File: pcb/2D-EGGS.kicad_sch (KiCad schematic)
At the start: 41 parts, among them J1 BUTTON 1, J10 EFFECT, J11 AUX, J12 USB_B, J13 PWAN1, J14 PWAN2, J15 ENCODER, J16 GPIO, J2 BUTTON 2, J3 BUTTON 3, J4 BUTTON 4, J5 BUTTON 5, J6 BUTTON 6, J7 BUTTON 7, J8 START, J9 VEFX, Q1 2N7000, Q10 2N7000, Q11 2N7000, Q2 2N7000, Q3 2N7000, Q4 2N7000, Q5 2N7000, Q6 2N7000, Q7 2N7000, Q8 2N7000, Q9 2N7000, SW1 SW_Push, U1 AT90USB1286, Y1 16MHz

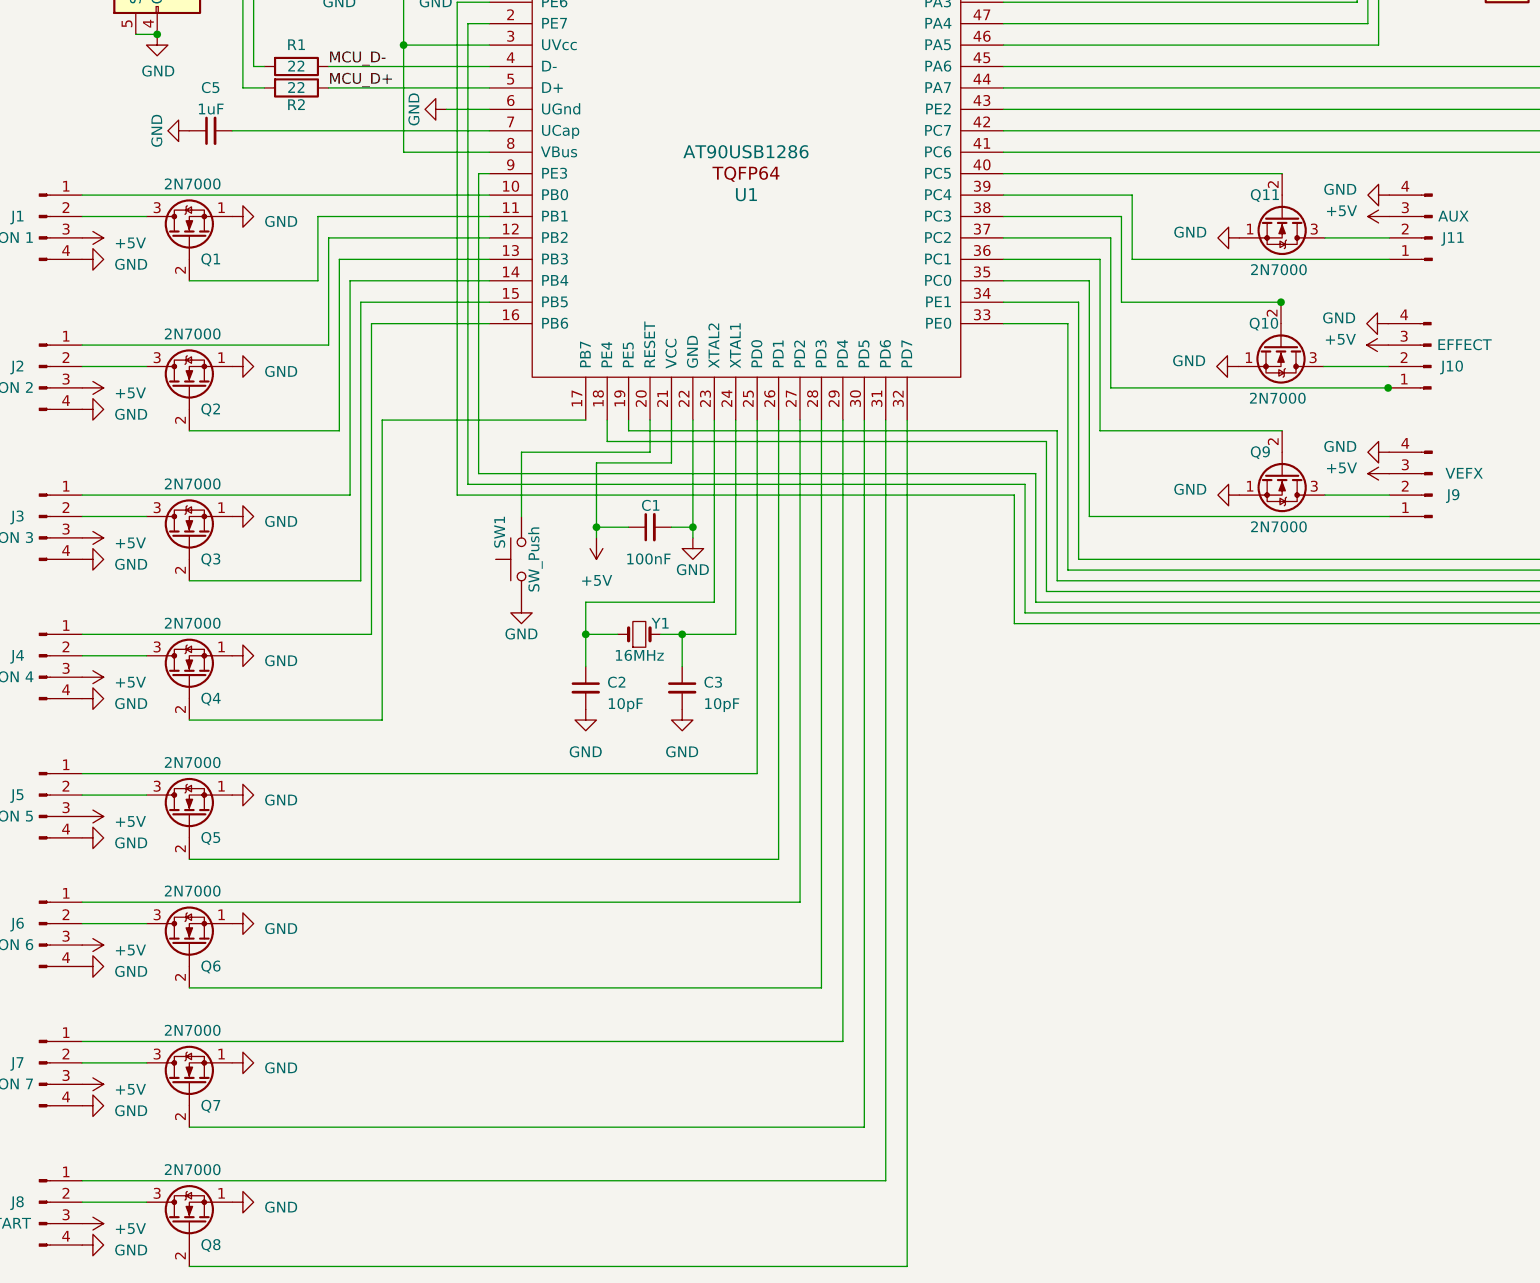
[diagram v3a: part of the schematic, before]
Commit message: 2N7000 -> 2N7002. add series resistor to reset switch
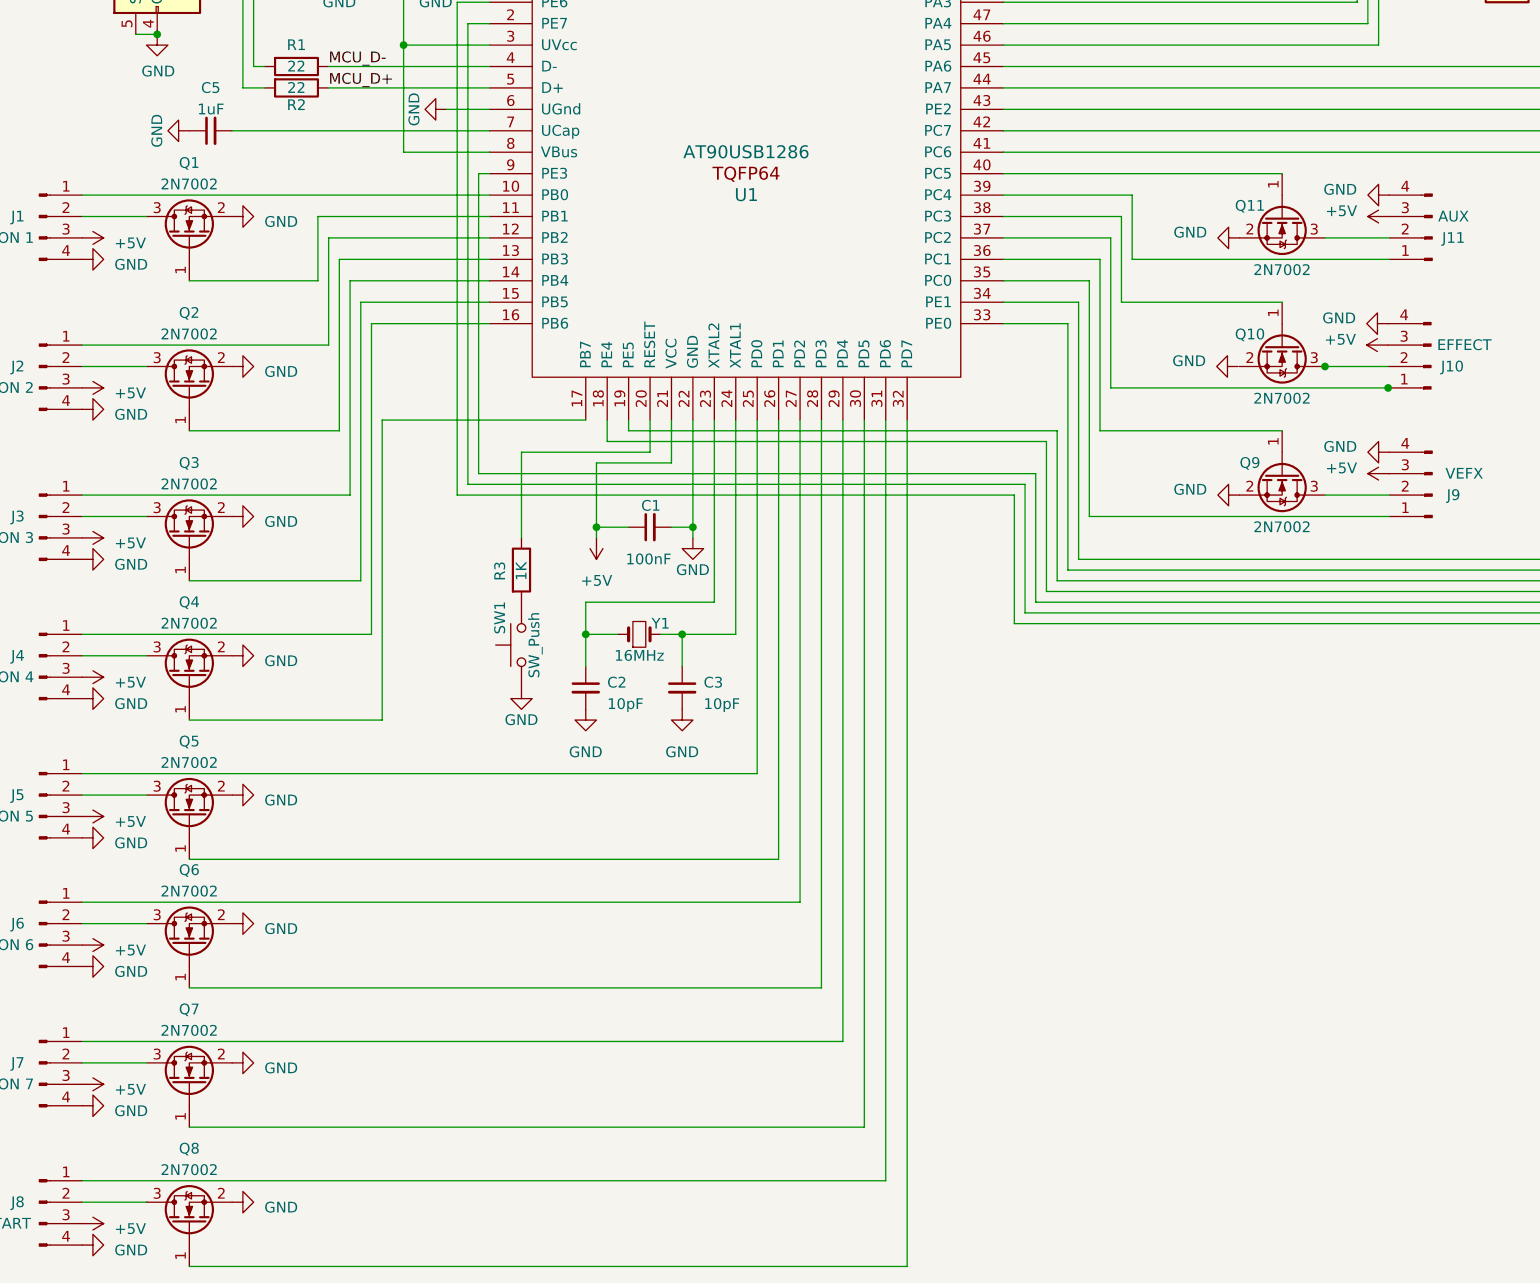
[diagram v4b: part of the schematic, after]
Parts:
- removed Q1, Q10, Q11, Q2, Q3, Q4, Q5, Q6, Q7, Q8, Q9: 2N7000, Package_TO_SOT_THT:TO-92_Inline, symbol Transistor_FET:2N7000
- added Q1, Q10, Q11, Q2, Q3, Q4, Q5, Q6, Q7, Q8, Q9: 2N7002, Package_TO_SOT_SMD:SOT-23, symbol Transistor_FET:2N7002
- added R3: 1K, Resistor_SMD:R_0805_2012Metric, symbol Device:R
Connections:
- net GND: now also Q1.2 (S), Q11.2 (S), Q2.2 (S), Q3.2 (S), Q4.2 (S), Q5.2 (S), Q6.2 (S), Q7.2 (S), Q8.2 (S), Q9.2 (S)
- net at J7.2 (Pin_2): now also Q7.3 (D)
- net at J2.2 (Pin_2): now also Q2.3 (D)
- net at J6.2 (Pin_2): now also Q6.3 (D)
- net at U1.15 (PB5): now also Q3.1 (G)
- net at J3.2 (Pin_2): now also Q3.3 (D)
- net at U1.38 (PC3): now also Q10.1 (G)
- net at J10.2 (Pin_2): now also Q10.3 (D)
- net at U1.28 (PD3): now also Q6.1 (G)
- net at J4.2 (Pin_2): now also Q4.3 (D)
- net at U1.40 (PC5): now also Q11.1 (G)
- net at J11.2 (Pin_2): now also Q11.3 (D)
- net at J9.2 (Pin_2): now also Q9.3 (D)
- net at U1.11 (PB1): now also Q1.1 (G)
- net at U1.13 (PB3): now also Q2.1 (G)
- net at U1.17 (PB7): now also Q4.1 (G)
- net at U1.20 (RESET): now also R3.1; no longer SW1.2
- net at U1.26 (PD1): now also Q5.1 (G)
- net at U1.30 (PD5): now also Q7.1 (G)
- net at U1.32 (PD7): now also Q8.1 (G)
- net at U1.36 (PC1): now also Q9.1 (G)
- net at J1.2 (Pin_2): now also Q1.3 (D)
- net at J5.2 (Pin_2): now also Q5.3 (D)
- net at J8.2 (Pin_2): now also Q8.3 (D)
- new net: R3.2, SW1.2
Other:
- moved on the sheet: SW1

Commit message: update schematic, pcb layout WIP
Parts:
- removed J1: BUTTON 1, Connector_JST:JST_XH_B4B-XH-A_1x04_P2.50mm_Vertical, symbol Connector:Conn_01x04_Pin
- removed J12: USB_B, Connector_USB:USB_B_OST_USB-B1HSxx_Horizontal, symbol jamma-streamer-rescue:USB_B-Connector
- removed J16: GPIO, Connector_PinHeader_2.54mm:PinHeader_2x12_P2.54mm_Vertical, symbol Connector_Generic:Conn_02x12_Counter_Clockwise
- removed J2: BUTTON 2, Connector_JST:JST_XH_B4B-XH-A_1x04_P2.50mm_Vertical, symbol Connector:Conn_01x04_Pin
- removed Q1, Q2: 2N7002, Package_TO_SOT_SMD:SOT-23, symbol Transistor_FET:2N7002
- added J1: ISP, Connector_PinHeader_2.54mm:PinHeader_2x03_P2.54mm_Vertical, symbol Connector_Generic:Conn_02x03_Odd_Even
- added J12: PWAN_CENTER_LED, Connector_JST:JST_XH_B3B-XH-A_1x03_P2.50mm_Vertical, symbol Connector:Conn_01x03_Pin
- added J16: DBG_PWR, Connector_PinHeader_2.54mm:PinHeader_1x02_P2.54mm_Vertical, symbol Connector_Generic:Conn_01x02
- added J17: PWAN_E2P1, Connector_JST:JST_XH_B3B-XH-A_1x03_P2.50mm_Vertical, symbol Connector:Conn_01x03_Pin
- added J18: PWAN_E2P2, Connector_JST:JST_XH_B3B-XH-A_1x03_P2.50mm_Vertical, symbol Connector:Conn_01x03_Pin
- added J19: ENCODER2, Connector_JST:JST_XH_B4B-XH-A_1x04_P2.50mm_Vertical, symbol Connector:Conn_01x04_Pin
- added J2: TT_LED, Connector_JST:JST_XH_B3B-XH-A_1x03_P2.50mm_Vertical, symbol Connector:Conn_01x03_Pin
- added J20: B10, Connector_JST:JST_XH_B4B-XH-A_1x04_P2.50mm_Vertical, symbol Connector:Conn_01x04_Pin
- added J21: B11, Connector_JST:JST_XH_B4B-XH-A_1x04_P2.50mm_Vertical, symbol Connector:Conn_01x04_Pin
- added J22: PWAN_USB_B, Connector_JST:JST_XH_B5B-XH-A_1x05_P2.50mm_Vertical, symbol Connector_Generic:Conn_01x05
- added J23: PWAN_USB_C, Connector_JST:JST_PH_B2B-PH-K_1x02_P2.00mm_Vertical, symbol Connector_Generic:Conn_01x02
- added J24: LED1, Connector_JST:JST_XH_B2B-XH-A_1x02_P2.50mm_Vertical, symbol Connector_Generic:Conn_01x02
- added J25: LED2, Connector_JST:JST_XH_B2B-XH-A_1x02_P2.50mm_Vertical, symbol Connector_Generic:Conn_01x02
- added P1: USB_C_DATA, Connector_USB:USB_C_Receptacle_GCT_USB4085, symbol Connector:USB_C_Plug
- added P2: USB_C_POWER, Connector_USB:USB_C_Receptacle_GCT_USB4085, symbol Connector:USB_C_Plug
- added Q12, Q13: 2N7002, Package_TO_SOT_SMD:SOT-23, symbol Transistor_FET:2N7002
- added R4: 4.7K, Resistor_SMD:R_0805_2012Metric, symbol Device:R
- J10: value EFFECT -> B8
- J11: value AUX -> B9
- J13: value PWAN1 -> PWAN_E1P1
- J14: value PWAN2 -> PWAN_E1P2
- J15: value ENCODER -> ENCODER1
- J3: value BUTTON 3 -> B1
- J4: value BUTTON 4 -> B2
- J5: value BUTTON 5 -> B3
- J6: value BUTTON 6 -> B4
- J7: value BUTTON 7 -> B5
- J8: value START -> B6
- J9: value VEFX -> B7
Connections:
- net +5V: now also J15.2 (Pin_2), J1.2 (Pin_2), J12.2 (Pin_2), J16.1 (Pin_1), J17.3 (Pin_3), J18.3 (Pin_3), J19.2 (Pin_2), J2.2 (Pin_2), J20.3 (Pin_3), J21.3 (Pin_3), J22.5 (Pin_5), J23.2 (Pin_2), J24.2 (Pin_2), J25.2 (Pin_2), P1.A4 (VBUS), P1.A9 (VBUS), P1.B4 (VBUS), P1.B9 (VBUS), P2.A4 (VBUS), P2.A9 (VBUS), P2.B4 (VBUS), P2.B9 (VBUS), R4.2; no longer J15.3 (Pin_3)
- net GND: now also J15.1 (Pin_1), J1.6 (Pin_6), J12.3 (Pin_3), J16.2 (Pin_2), J17.2 (Pin_2), J18.2 (Pin_2), J19.1 (Pin_1), J2.3 (Pin_3), J20.4 (Pin_4), J21.4 (Pin_4), J22.1 (Pin_1), J22.2 (Pin_2), J23.1 (Pin_1), J24.1 (Pin_1), J25.1 (Pin_1), P1.A1 (GND), P1.A12 (GND), P1.B1 (GND), P1.B12 (GND), P1.S1 (SHIELD), P2.A1 (GND), P2.A12 (GND), P2.B1 (GND), P2.B12 (GND), P2.S1 (SHIELD), Q12.2 (S), Q13.2 (S); no longer J15.4 (Pin_4)
- net USB-R_D+: now also J22.3 (Pin_3), P1.A6 (D+)
- net USB-R_D-: now also J22.4 (Pin_4), P1.A7 (D-)
- net at U1.12 (PB2_MOSI): now also J1.4 (Pin_4)
- net at J13.1 (Pin_1), U1.61 (PF0): now also J15.4 (Pin_4); no longer J15.1 (Pin_1)
- net at J14.1 (Pin_1), U1.60 (PF1): now also J15.3 (Pin_3); no longer J15.2 (Pin_2)
- net at Q10.1 (G): now also U1.36 (PC1); no longer U1.38 (PC3)
- net at J9.1 (Pin_1): now also U1.33 (PE0); no longer U1.35 (PC0)
- net at U1.11 (PB1_SCLK): now also J1.3 (Pin_3)
- net at U1.13 (PB3_MISO): now also J1.1 (Pin_1)
- net at R3.1, U1.20 (RESET): now also J1.5 (Pin_5), R4.1
- net at U1.34 (PE1): now also Q9.1 (G)
- net at J10.1 (Pin_1): now also U1.35 (PC0); no longer U1.37 (PC2)
- net at U1.39 (PC4): now also J12.1 (Pin_1); no longer J11.1 (Pin_1)
- net at Q11.1 (G): now also U1.38 (PC3); no longer U1.40 (PC5)
- net at U1.43 (PE2): now also J20.1 (Pin_1)
- net at U1.44 (PA7): now also Q12.1 (G)
- net at U1.45 (PA6): now also J21.1 (Pin_1)
- net at U1.46 (PA5): now also Q13.1 (G)
- net at U1.58 (PF3): now also J18.1 (Pin_1), J19.3 (Pin_3)
- net at U1.59 (PF2): now also J17.1 (Pin_1), J19.4 (Pin_4)
- new net: J20.2 (Pin_2), Q12.3 (D)
- new net: J21.2 (Pin_2), Q13.3 (D)
- new net: J11.1 (Pin_1), U1.37 (PC2)
- new net: J2.1 (Pin_1), U1.40 (PC5)
- no-connect marks 0 -> 43
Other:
- moved on the sheet: C1, C2, C3, C4, C5, C6, C7, C8, C9, J10, J11, J13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

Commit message: v2 routed
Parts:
- added J26: APWR, Connector_PinHeader_2.54mm:PinHeader_1x02_P2.54mm_Vertical, symbol Connector_Generic:Conn_01x02
- J16: value DBG_PWR -> DPWR
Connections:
- net +5V: now also J26.1 (Pin_1)
- net GND: now also J26.2 (Pin_2)
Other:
- moved on the sheet: J16
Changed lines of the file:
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@@
     )
   )
-  (symbol (lib_id "power:GND") (at 247.65 194.31 90) (unit 1)
-    (in_bom yes) (on_board yes) (dnp no) (fields_autoplaced)
-    (property "Reference" "#PWR072" (at 254 194.31 0)
-      (effects (font (size 1.27 1.27)) hide)
-    )
-    (property "Value" "GND" (at 251.46 193.675 90)
-      (effects (font (size 1.27 1.27)) (justify right))
-    )
-    (property "Footprint" "" (at 247.65 194.31 0)
-      (effects (font (size 1.27 1.27)) hide)
-    )
-    (property "Datasheet" "" (at 247.65 194.31 0)
+  (symbol (lib_id "power:GND") (at 247.65 195.58 90) (unit 1)
+    (in_bom yes) (on_board yes) (dnp no) (fields_autoplaced)
+    (property "Reference" "#PWR072" (at 254 195.58 0)
+      (effects (font (size 1.27 1.27)) hide)
+    )
+    (property "Value" "GND" (at 251.46 194.945 90)
+      (effects (font (size 1.27 1.27)) (justify right))
+    )
+    (property "Footprint" "" (at 247.65 195.58 0)
+      (effects (font (size 1.27 1.27)) hide)
+    )
+    (property "Datasheet" "" (at 247.65 195.58 0)
       (effects (font (size 1.27 1.27)) hide)
     )
@@
     )
   )
+  (symbol (lib_id "Connector_Generic:Conn_01x02") (at 242.57 189.23 180) (unit 1)
+    (in_bom yes) (on_board yes) (dnp no)
+    (property "Reference" "J26" (at 242.57 184.15 0)
+      (effects (font (size 1.27 1.27)))
+    )
+    (property "Value" "APWR" (at 237.49 187.96 0)
+      (effects (font (size 1.27 1.27)))
+    )
+    (property "Footprint" "Connector_PinHeader_2.54mm:PinHeader_1x02_P2.54mm_Vertical" (at 242.57 189.23 0)
+      (effects (font (size 1.27 1.27)) hide)
+    )
+    (property "Datasheet" "~" (at 242.57 189.23 0)
+      (effects (font (size 1.27 1.27)) hide)
+    )
+    (pin "1")
+    (pin "2")
+    (instances
+      (project "2D-EGGS"
+        (path "/603cab36-5bc1-4050-9595-d50dcdf15559"
+          (reference "J26") (unit 1)
+        )
+      )
+    )
+  )
+  (symbol (lib_id "power:+5V") (at 247.65 189.23 270) (unit 1)
+    (in_bom yes) (on_board yes) (dnp no) (fields_autoplaced)
+    (property "Reference" "#PWR084" (at 243.84 189.23 0)
+      (effects (font (size 1.27 1.27)) hide)
+    )
+    (property "Value" "+5V" (at 251.46 189.865 90)
+      (effects (font (size 1.27 1.27)) (justify left))
+    )
+    (property "Footprint" "" (at 247.65 189.23 0)
+      (effects (font (size 1.27 1.27)) hide)
+    )
+    (property "Datasheet" "" (at 247.65 189.23 0)
+      (effects (font (size 1.27 1.27)) hide)
+    )
+    (pin "1")
+    (instances
+      (project "2D-EGGS"
+        (path "/603cab36-5bc1-4050-9595-d50dcdf15559"
+          (reference "#PWR084") (unit 1)
+        )
+      )
+    )
+  )
+  (symbol (lib_id "power:GND") (at 247.65 186.69 90) (unit 1)
+    (in_bom yes) (on_board yes) (dnp no) (fields_autoplaced)
+    (property "Reference" "#PWR083" (at 254 186.69 0)
+      (effects (font (size 1.27 1.27)) hide)
+    )
+    (property "Value" "GND" (at 251.46 186.055 90)
+      (effects (font (size 1.27 1.27)) (justify right))
+    )
+    (property "Footprint" "" (at 247.65 186.69 0)
+      (effects (font (size 1.27 1.27)) hide)
+    )
+    (property "Datasheet" "" (at 247.65 186.69 0)
+      (effects (font (size 1.27 1.27)) hide)
+    )
+    (pin "1")
+    (instances
+      (project "2D-EGGS"
+        (path "/603cab36-5bc1-4050-9595-d50dcdf15559"
+          (reference "#PWR083") (unit 1)
+        )
+      )
+    )
+  )
   (symbol (lib_id "power:+5V") (at 217.17 68.58 180) (unit 1)
     (in_bom yes) (on_board yes) (dnp no)
@@
     )
   )
-  (symbol (lib_id "power:+5V") (at 247.65 196.85 270) (unit 1)
-    (in_bom yes) (on_board yes) (dnp no) (fields_autoplaced)
-    (property "Reference" "#PWR073" (at 243.84 196.85 0)
-      (effects (font (size 1.27 1.27)) hide)
-    )
-    (property "Value" "+5V" (at 251.46 197.485 90)
-      (effects (font (size 1.27 1.27)) (justify left))
-    )
-    (property "Footprint" "" (at 247.65 196.85 0)
-      (effects (font (size 1.27 1.27)) hide)
-    )
-    (property "Datasheet" "" (at 247.65 196.85 0)
+  (symbol (lib_id "power:+5V") (at 247.65 198.12 270) (unit 1)
+    (in_bom yes) (on_board yes) (dnp no) (fields_autoplaced)
+    (property "Reference" "#PWR073" (at 243.84 198.12 0)
+      (effects (font (size 1.27 1.27)) hide)
+    )
+    (property "Value" "+5V" (at 251.46 198.755 90)
+      (effects (font (size 1.27 1.27)) (justify left))
+    )
+    (property "Footprint" "" (at 247.65 198.12 0)
+      (effects (font (size 1.27 1.27)) hide)
+    )
+    (property "Datasheet" "" (at 247.65 198.12 0)
       (effects (font (size 1.27 1.27)) hide)
     )
@@
     )
   )
-  (symbol (lib_id "Connector_Generic:Conn_01x02") (at 242.57 196.85 180) (unit 1)
-    (in_bom yes) (on_board yes) (dnp no) (fields_autoplaced)
-    (property "Reference" "J16" (at 240.03 196.215 0)
-      (effects (font (size 1.27 1.27)) (justify left))
-    )
-    (property "Value" "DBG_PWR" (at 240.03 193.675 0)
-      (effects (font (size 1.27 1.27)) (justify left))
-    )
-    (property "Footprint" "Connector_PinHeader_2.54mm:PinHeader_1x02_P2.54mm_Vertical" (at 242.57 196.85 0)
-      (effects (font (size 1.27 1.27)) hide)
-    )
-    (property "Datasheet" "~" (at 242.57 196.85 0)
-      (effects (font (size 1.27 1.27)) hide)
-    )
+  (symbol (lib_id "Connector_Generic:Conn_01x02") (at 242.57 198.12 180) (unit 1)
+    (in_bom yes) (on_board yes) (dnp no)
+    (property "Reference" "J16" (at 242.57 193.04 0)
+      (effects (font (size 1.27 1.27)))
+    )
+    (property "Value" "DPWR" (at 237.49 196.85 0)
+      (effects (font (size 1.27 1.27)))
+    )
+    (property "Footprint" "Connector_PinHeader_2.54mm:PinHeader_1x02_P2.54mm_Vertical" (at 242.57 198.12 0)
+      (effects (font (size 1.27 1.27)) hide)
+    )
+    (property "Datasheet" "~" (at 242.57 198.12 0)
+      (effects (font (size 1.27 1.27)) hide)
+    )

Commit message: update connector enumuration to match standard iidx controller layout
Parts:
- J10: value B8 -> B10
- J11: value B9 -> B8
- J20: value B10 -> B9
- J4: value B2 -> B6
- J8: value B6 -> B2
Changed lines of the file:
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@@
       (effects (font (size 1.27 1.27)))
     )
-    (property "Value" "B10" (at 271.78 120.65 0)
+    (property "Value" "B9" (at 271.78 120.65 0)
       (effects (font (size 1.27 1.27)))
     )
@@
       (effects (font (size 1.27 1.27)))
     )
-    (property "Value" "B2" (at 100.33 193.04 0)
+    (property "Value" "B6" (at 100.33 193.04 0)
       (effects (font (size 1.27 1.27)))
     )
@@
       (effects (font (size 1.27 1.27)))
     )
-    (property "Value" "B9" (at 271.78 143.51 0)
+    (property "Value" "B8" (at 271.78 143.51 0)
       (effects (font (size 1.27 1.27)))
     )
@@
       (effects (font (size 1.27 1.27)))
     )
-    (property "Value" "B6" (at 100.33 257.81 0)
+    (property "Value" "B2" (at 100.33 257.81 0)
       (effects (font (size 1.27 1.27)))
     )
@@
       (effects (font (size 1.27 1.27)))
     )
-    (property "Value" "B8" (at 271.78 158.75 0)
+    (property "Value" "B10" (at 271.78 158.75 0)
       (effects (font (size 1.27 1.27)))
     )
